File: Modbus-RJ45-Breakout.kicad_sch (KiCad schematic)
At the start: 99 parts, among them J1 RJ45_Weidmueller_2562920000, J2 RJ45_Weidmueller_2562920000, J3 Conn_01x04, J4 Conn_01x04, J5 USB_B_Mini, U2 WE-TVS-82400102, U3 MAX485E, U4 ADM2687E, U7 MAX485E, U8 ADM2687E

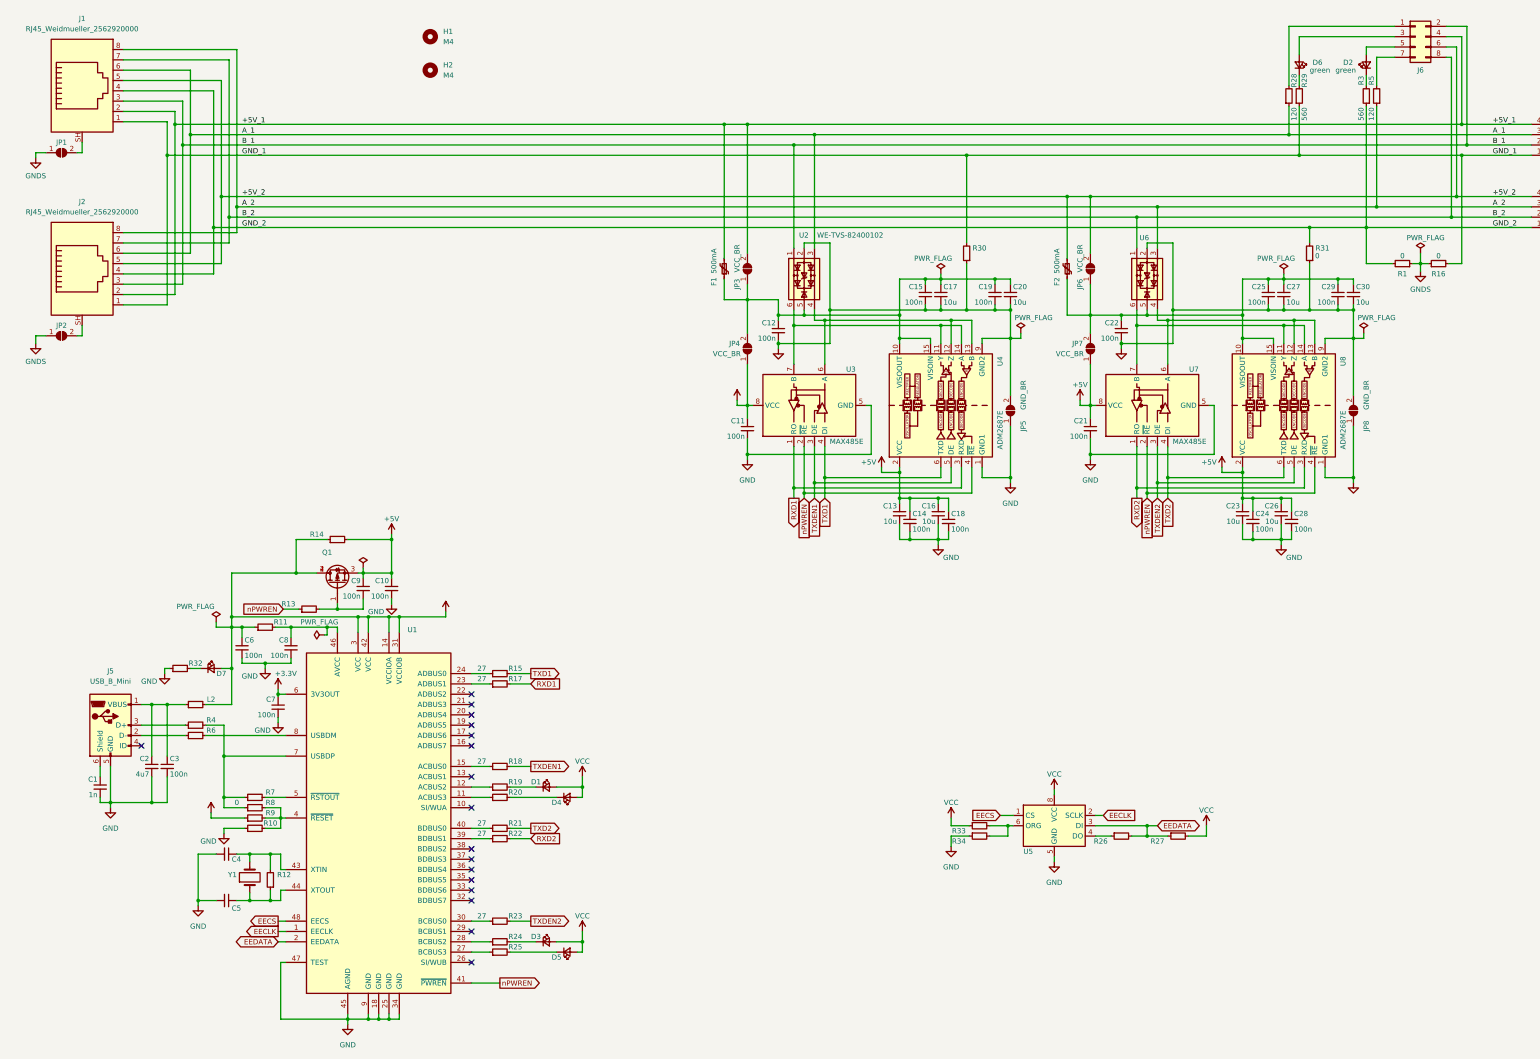
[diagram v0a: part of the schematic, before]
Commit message: Partly improved and re-routed
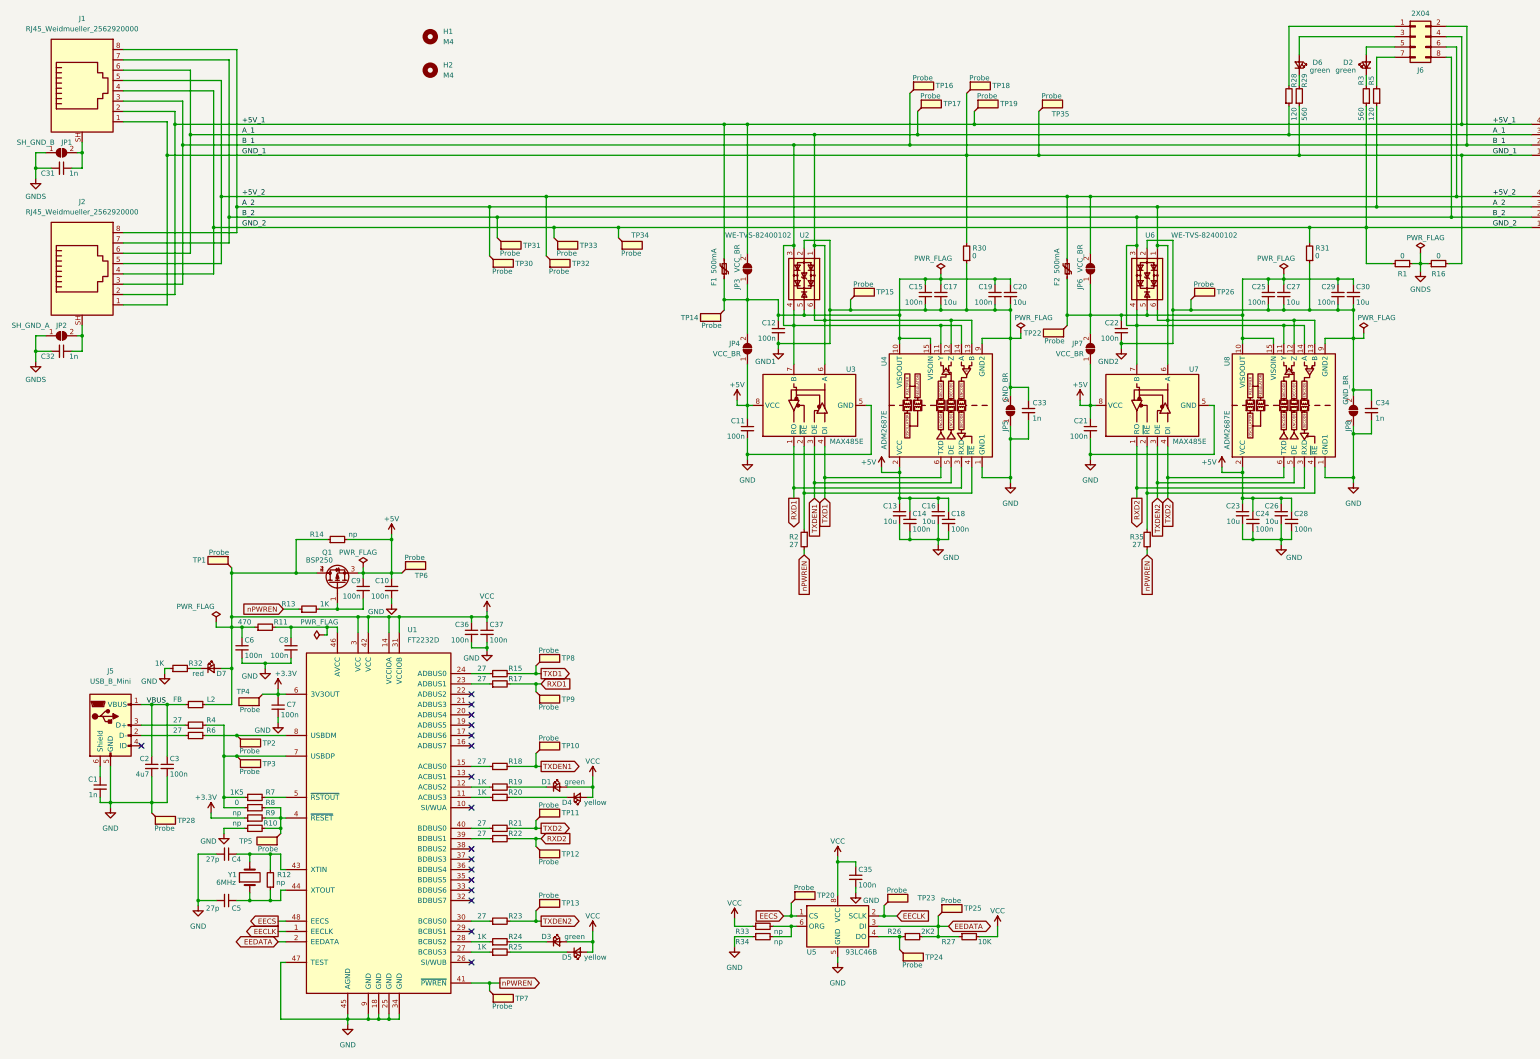
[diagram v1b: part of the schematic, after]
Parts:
- added C31, C32, C33, C34: 1n, Capacitor_SMD:C_1206_3216Metric_Pad1.33x1.80mm_HandSolder, symbol Device:C_Small
- added C35, C36, C37: 100n, Capacitor_SMD:C_0603_1608Metric_Pad1.08x0.95mm_HandSolder, symbol Device:C_Small
- added R2, R35: 27, Resistor_SMD:R_0603_1608Metric_Pad0.98x0.95mm_HandSolder, symbol Device:R_Small
- added TP1, TP28, TP34, TP35, TP6: Probe, TestPoint:TestPoint_THTPad_2.0x2.0mm_Drill1.0mm, symbol Connector:TestPoint_Flag
- added TP10, TP11, TP12, TP13, TP14, TP15, TP16, TP17, TP18, TP19, TP2, TP20, TP22, TP23, TP24, TP25, TP26, TP3, TP30, TP31, TP32, TP33, TP4, TP5, TP7, TP8, TP9: Probe, TestPoint:TestPoint_Pad_D1.5mm, symbol Connector:TestPoint_Flag
- C4, C5: value (none) -> 27p; footprint (none) -> Capacitor_SMD:C_0603_1608Metric_Pad1.08x0.95mm_HandSolder
- D1, D3: value (none) -> green; footprint (none) -> LED_SMD:LED_0603_1608Metric_Pad1.05x0.95mm_HandSolder
- D4, D5: value (none) -> yellow; footprint (none) -> LED_SMD:LED_0603_1608Metric_Pad1.05x0.95mm_HandSolder
- D7: value (none) -> red; footprint (none) -> LED_SMD:LED_0603_1608Metric_Pad1.05x0.95mm_HandSolder
- J3, J4: footprint Connector_Wago:Wago_734-164_1x04_P3.50mm_Horizontal -> the78mole:Wago_734-164_1x04_P3.50mm_Horizontal
- J5: footprint Connector_USB:USB_Mini-B_Wuerth_65100516121_Horizontal -> the78mole:USB_Mini-B_Wuerth_65100516121_Horizontal
- J6: value (none) -> 2X04; footprint (none) -> Connector_PinHeader_2.54mm:PinHeader_2x04_P2.54mm_Vertical_SMD
- JP1: value (none) -> SH_GND_B; footprint (none) -> Jumper:SolderJumper-2_P1.3mm_Open_TrianglePad1.0x1.5mm
- JP2: value (none) -> SH_GND_A; footprint (none) -> Jumper:SolderJumper-2_P1.3mm_Open_TrianglePad1.0x1.5mm
- L2: value (none) -> FB; footprint (none) -> Resistor_SMD:R_0603_1608Metric_Pad0.98x0.95mm_HandSolder
- Q1: value (none) -> BSP250; footprint (none) -> Package_TO_SOT_SMD:SOT-223
- R10, R12, R14, R33, R34, R9: value (none) -> np; footprint (none) -> Resistor_SMD:R_0603_1608Metric_Pad0.98x0.95mm_HandSolder
- R11: value (none) -> 470; footprint (none) -> Resistor_SMD:R_0603_1608Metric_Pad0.98x0.95mm_HandSolder
- R13, R19, R20, R24, R25, R32: value (none) -> 1K; footprint (none) -> Resistor_SMD:R_0603_1608Metric_Pad0.98x0.95mm_HandSolder
- R26: value (none) -> 2K2; footprint (none) -> Resistor_SMD:R_0603_1608Metric_Pad0.98x0.95mm_HandSolder
- R27: value (none) -> 10K; footprint (none) -> Resistor_SMD:R_0603_1608Metric_Pad0.98x0.95mm_HandSolder
- R30: value (none) -> 0; footprint (none) -> Resistor_SMD:R_0603_1608Metric_Pad0.98x0.95mm_HandSolder
- R4, R6: value (none) -> 27; footprint (none) -> Resistor_SMD:R_0603_1608Metric_Pad0.98x0.95mm_HandSolder
- R7: value (none) -> 1K5; footprint (none) -> Resistor_SMD:R_0603_1608Metric_Pad0.98x0.95mm_HandSolder
- U1: value (none) -> FT2232D; footprint (none) -> Package_QFP:LQFP-48_7x7mm_P0.5mm
- U5: value (none) -> 93LC46B; footprint (none) -> Package_SO:SOIC-8_3.9x4.9mm_P1.27mm
- U6: value (none) -> WE-TVS-82400102; footprint (none) -> Package_TO_SOT_SMD:SOT-23-6
- Y1: value (none) -> 6MHz; footprint (none) -> Crystal:Crystal_SMD_HC49-SD_HandSoldering
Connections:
- net +3V3: now also TP4.1
- net +5V: now also TP6.1
- net +5V_1: now also TP19.1
- net +5V_2: now also TP32.1
- net A_1: now also U2.1, U2.6, U3.6 (A), U4.12 (Z), U4.13 (B), TP17.1; no longer U2.3
- net A_2: now also U6.1, U6.6, U7.6 (A), U8.12 (Z), U8.13 (B), TP30.1; no longer U6.3
- net B_1: now also U2.3, U2.4, U3.7 (B), U4.11 (Y), U4.14 (A), TP16.1; no longer U2.1
- net B_2: now also U6.3, U6.4, U7.7 (B), U8.11 (Y), U8.14 (A), TP31.1; no longer U6.1
- net EECLK: now also TP23.1
- net EECS: now also TP20.1
- net EEDATA: now also TP25.1
- net GND: now also C33.2, C34.2, C35.2, C36.2, C37.2, TP28.1
- net GND1: now also C33.1, TP15.1
- net GND2: now also C34.1, TP26.1
- net GNDS: now also C31.2, C32.2
- net GND_1: now also TP18.1, TP35.1
- net GND_2: now also TP33.1, TP34.1
- net RXD1: now also TP9.1
- net RXD2: now also TP12.1
- net TXD1: now also TP8.1
- net TXD2: now also TP11.1
- net TXDEN1: now also TP10.1
- net TXDEN2: now also TP13.1
- net VCC: now also C35.1, C36.1, C37.1, TP1.1
- net nPWREN: now also R2.2, R35.2, TP7.1; no longer U3.2 (~{RE}), U4.4 (~{RE}), U7.2 (~{RE}), U8.4 (~{RE})
- net at C12.1, C15.1, C17.1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: now also TP14.1
- net at C22.1, C25.1, C27.1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: now also TP22.1
- net at R4.2, R7.1, R8.1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: now also TP3.1
- net at R10.2, R8.2, R9.2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: now also TP5.1
- net at J1.SH, JP1.2 (B): now also C31.1
- net at R26.1, U5.4 (DO): now also TP24.1
- net VBUS: now reaches C2.1, C3.1, J5.1 (VBUS), L2.1
- net at J2.SH, JP2.2 (B): now also C32.1
- net at R6.2, U1.8 (USBDM): now also TP2.1
- new net: R35.1, U7.2 (~{RE}), U8.4 (~{RE})
- new net: R2.1, U3.2 (~{RE}), U4.4 (~{RE})
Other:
- moved on the sheet: D1, D3, D4, D5, R26, R27, R33, R34, U2, U5, U6

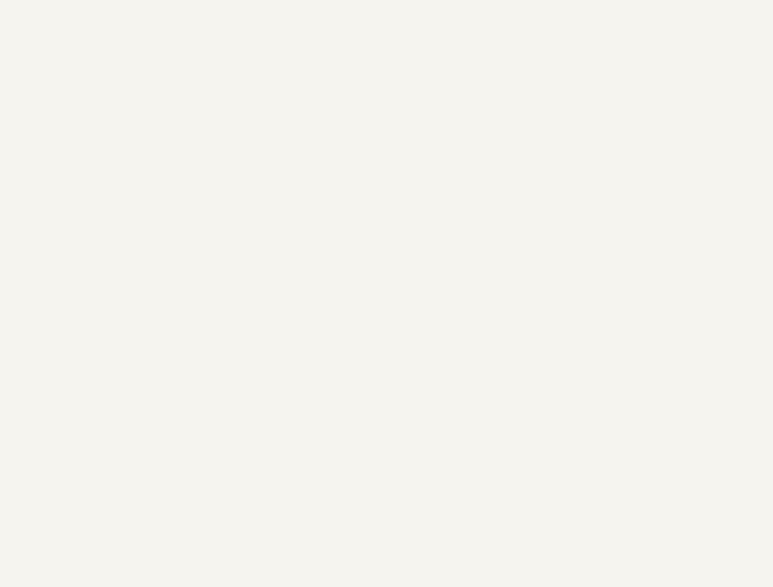
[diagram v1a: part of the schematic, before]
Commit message: As ordered, added info on enclosures
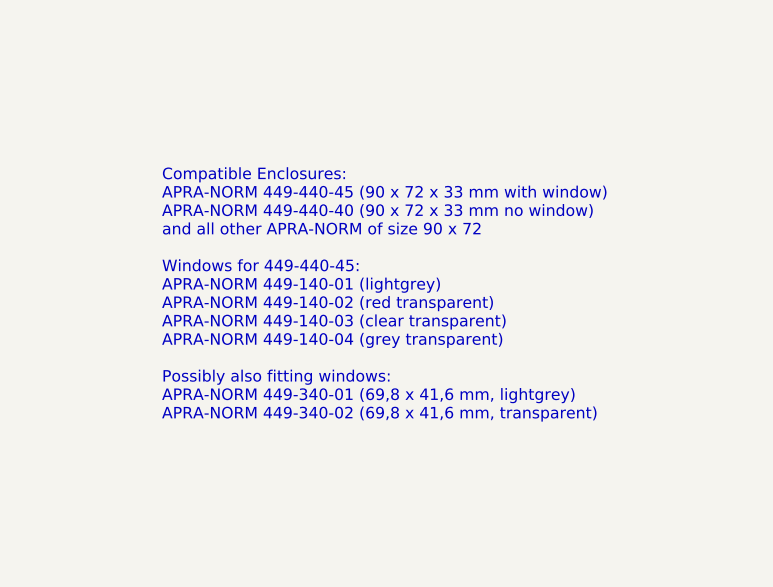
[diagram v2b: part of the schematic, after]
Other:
- note added: "Compatible Enclosures: APRA-NORM 449-440-45 (90 x 72 x 33 mm with window) APRA-NORM 449-440-40 (90 x 72 x 33 mm no window) and all other APRA-NORM of size 90 x 72 Windows for 449-440-45: APRA-NORM 449-140-01 (lightgrey) APRA-NORM 449-140-02 (red transparent) APRA-NORM 449-140-03 (clear transparent) APRA-NORM 449-140-04 (grey transparent) Possibly also fitting windows: APRA-NORM 449-340-01 (69,8 x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"
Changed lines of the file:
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@@
     (stroke (width 0) (type default) (color 0 0 0 0))
+  )
+  (text "Compatible Enclosures:\nAPRA-NORM 449-440-45 (90 x 72 x 33 mm with window)\nAPRA-NORM 449-440-40 (90 x 72 x 33 mm no window)\nand all other APRA-NORM of size 90 x 72\n\nWindows for 449-440-45:\nAPRA-NORM 449-140-01 (lightgrey)\nAPRA-NORM 449-140-02 (red transparent)\nAPRA-NORM 449-140-03 (clear transparent)\nAPRA-NORM 449-140-04 (grey transparent)\n\nPossibly also fitting windows:\nAPRA-NORM 449-340-01 (69,8 x 41,6 mm, lightgrey)\nAPRA-NORM 449-340-02 (69,8 x 41,6 mm, transparent)\n\n\n"
+    (at 343.535 250.825 0)
+    (effects (font (size 1.27 1.27)) (justify left bottom))
   )
   (label "VBUS" (at 45.72 185.42 0)

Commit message: Fixed TP docs on PCB and added ibom
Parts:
- Y1: Reichelt (none) -> IQD LFXTAL016788
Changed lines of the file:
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@@
+      (effects (font (size 1.27 1.27)) hide)
+    )
+    (property "Reichelt" "IQD LFXTAL016788" (id 7) (at 71.12 227.965 90)
       (effects (font (size 1.27 1.27)) hide)
     )

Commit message: Adjustments during prototype build
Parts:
- R29, R3: value 560 -> (none); footprint Resistor_SMD:R_0603_1608Metric_Pad0.98x0.95mm_HandSolder -> (none)
- R8: value 0 -> (none); footprint Resistor_SMD:R_0603_1608Metric_Pad0.98x0.95mm_HandSolder -> (none)
- R9: value np -> (none); footprint Resistor_SMD:R_0603_1608Metric_Pad0.98x0.95mm_HandSolder -> (none)
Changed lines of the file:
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@@
     (in_bom yes) (on_board yes)
     (property "Reference" "R8" (id 0) (at 76.2 209.55 90))
-    (property "Value" "0" (id 1) (at 67.945 209.55 90))
-    (property "Footprint" "Resistor_SMD:R_0603_1608Metric_Pad0.98x0.95mm_HandSolder" (id 2) (at 72.39 210.82 0)
+    (property "Value" "" (id 1) (at 67.945 209.55 90))
+    (property "Footprint" "" (id 2) (at 72.39 210.82 0)
       (effects (font (size 1.27 1.27)) hide)
     )
@@
     (in_bom yes) (on_board yes)
     (property "Reference" "R3" (id 0) (at 344.805 31.75 90))
-    (property "Value" "560" (id 1) (at 344.805 40.005 90))
-    (property "Footprint" "Resistor_SMD:R_0603_1608Metric_Pad0.98x0.95mm_HandSolder" (id 2) (at 346.075 35.56 0)
+    (property "Value" "" (id 1) (at 344.805 40.005 90))
+    (property "Footprint" "" (id 2) (at 346.075 35.56 0)
       (effects (font (size 1.27 1.27)) hide)
     )
@@
     (in_bom yes) (on_board yes)
     (property "Reference" "R29" (id 0) (at 330.835 31.75 90))
-    (property "Value" "560" (id 1) (at 330.835 40.005 90))
-    (property "Footprint" "Resistor_SMD:R_0603_1608Metric_Pad0.98x0.95mm_HandSolder" (id 2) (at 329.565 35.56 0)
+    (property "Value" "" (id 1) (at 330.835 40.005 90))
+    (property "Footprint" "" (id 2) (at 329.565 35.56 0)
       (effects (font (size 1.27 1.27)) hide)
     )
@@
     (in_bom yes) (on_board yes)
     (property "Reference" "R9" (id 0) (at 76.2 212.09 90))
-    (property "Value" "np" (id 1) (at 67.945 212.09 90))
-    (property "Footprint" "Resistor_SMD:R_0603_1608Metric_Pad0.98x0.95mm_HandSolder" (id 2) (at 72.39 213.36 0)
+    (property "Value" "" (id 1) (at 67.945 212.09 90))
+    (property "Footprint" "" (id 2) (at 72.39 213.36 0)
       (effects (font (size 1.27 1.27)) hide)
     )
@@
     )
     (path "/14c667e2-48bf-486f-835f-2bfc8b1b68a9"
-      (reference "R3") (unit 1) (value "560") (footprint "Resistor_SMD:R_0603_1608Metric_Pad0.98x0.95mm_HandSolder")
+      (reference "R3") (unit 1) (value "1K") (footprint "Resistor_SMD:R_0603_1608Metric_Pad0.98x0.95mm_HandSolder")
     )
     (path "/ffba077d-789a-43fd-9690-fea8d1c6c6e3"
@@
     )
     (path "/0ce16148-6e5c-406f-b93f-5f9bdea40745"
-      (reference "R8") (unit 1) (value "0") (footprint "Resistor_SMD:R_0603_1608Metric_Pad0.98x0.95mm_HandSolder")
+      (reference "R8") (unit 1) (value "np") (footprint "Resistor_SMD:R_0603_1608Metric_Pad0.98x0.95mm_HandSolder")
     )
     (path "/e9bfecd0-abec-4635-bba6-51fe95cde897"
-      (reference "R9") (unit 1) (value "np") (footprint "Resistor_SMD:R_0603_1608Metric_Pad0.98x0.95mm_HandSolder")
+      (reference "R9") (unit 1) (value "1K5") (footprint "Resistor_SMD:R_0603_1608Metric_Pad0.98x0.95mm_HandSolder")
     )
     (path "/b78bd01a-2206-46d8-905f-796ed73c744b"
@@
     )
     (path "/88437f4a-27c1-4b04-98c4-1a971c51d440"
-      (reference "R29") (unit 1) (value "560") (footprint "Resistor_SMD:R_0603_1608Metric_Pad0.98x0.95mm_HandSolder")
+      (reference "R29") (unit 1) (value "1K") (footprint "Resistor_SMD:R_0603_1608Metric_Pad0.98x0.95mm_HandSolder")
     )
     (path "/ec52c643-6bf7-4767-a00c-6c226ebdebc9"

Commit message: RS485 bus echo solved and A<->B swap with ISO Transceivers (schematic only)
This can be solved also with the current PCB by swapping the A and B externally
and not mixing ISO and non-ISO bus transceivers. The RX-Enable problem can be solved
by a desoldering R2 and R35 and bridging the pads to R18 and R23 resp. close to the transceiver.
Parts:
- added R? (x2): 27, Resistor_SMD:R_0603_1608Metric_Pad0.98x0.95mm_HandSolder, symbol Device:R_Small
- R2: value 27 -> (none); footprint Resistor_SMD:R_0603_1608Metric_Pad0.98x0.95mm_HandSolder -> (none)
- R29, R3: value (none) -> 1K; footprint (none) -> Resistor_SMD:R_0603_1608Metric_Pad0.98x0.95mm_HandSolder
- R35: value 27 -> (none); footprint Resistor_SMD:R_0603_1608Metric_Pad0.98x0.95mm_HandSolder -> (none); NP (none) -> np
- R8: value (none) -> np; footprint (none) -> Resistor_SMD:R_0603_1608Metric_Pad0.98x0.95mm_HandSolder
- R9: value (none) -> 1K5; footprint (none) -> Resistor_SMD:R_0603_1608Metric_Pad0.98x0.95mm_HandSolder
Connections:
- net A_1: now also U4.11 (Y), U4.14 (A); no longer U4.12 (Z), U4.13 (B)
- net A_2: now also U8.11 (Y), U8.14 (A); no longer U8.12 (Z), U8.13 (B)
- net B_1: now also U4.12 (Z), U4.13 (B); no longer U4.11 (Y), U4.14 (A)
- net B_2: now also U8.12 (Z), U8.13 (B); no longer U8.11 (Y), U8.14 (A)
- net TXDEN1: now also R?.2
- net TXDEN2: now also R?.2
- net at R35.1, U7.2 (~{RE}), U8.4 (~{RE}): now also R?.1
- net at R2.1, U3.2 (~{RE}), U4.4 (~{RE}): now also R?.1
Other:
- note added: "TODO: Update PCB"
- note added: "This is just optional, if you want to provide a different manufacturer or device identifier or want to change the maximum current drawn from USB bus. To program it, you can get the FT_PROG - EEPROM Programming Utility from FTDI (current version: 3.12.31.639). https://ftdichip.com/utilities/"
- note added: "This is the suggested solution from FT2232D datasheet to get RS485 interfaces. But it does not work well with wide spread ModBus libraries, which can not filter the echo from the bus. Therefore, the RX-enable (nRE) must be connected with TX-enable (DI/DE) to mask the transmit data from RX."
- moved on the sheet: R2, R35

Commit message: Fixed all issues and added Gerber exports
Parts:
- added DRA1: APRA 449-440-45, symbol Mechanical:DIN_Rail_Adapter
- added J7: WAGO 2734-104, symbol Connector:Conn_01x04_Female
- added J8: (no value), symbol Connector:Conn_01x04_Female
- J3: value Conn_01x04 -> Bus_2
- J4: value Conn_01x04 -> BUS_1
- R2, R35: value (none) -> np; footprint (none) -> Resistor_SMD:R_0603_1608Metric_Pad0.98x0.95mm_HandSolder
- gave numbers to parts that had none: 2
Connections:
- net A_2: now also U6.3, U6.4; no longer U6.1, U6.6
- net B_2: now also U6.1, U6.6; no longer U6.3, U6.4
- no-connect marks 17 -> 25
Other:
- note added: "Mating connectors: 2 x WAGO 2734-104"
- note added: "R2 and R35 have been the suggested solution from FT2232D datasheet to realize RS485 interfaces. But it does not work well with wide spread ModBus SW libraries, which can not filter the echo from the bus. Therefore, the RX-enable (nRE) must be connected with TX-enable (DI/DE) by R36 and R37 to mask the transmit data from RX."
- note added: "When using the isolated RS485 Transceiver (ADM2687E) it is not recommended to bridge the power to the bus. This has two reasons: 1. The power capability of the ISO power is 55 mA while the requirement of the isolated side can reach up to 55 mA on worst operating conditions (highest data rate (16 MBps), highest operating temperature and lowest termination: 54 Ohms total = 2 x 120 Ohms + loads 2. T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"
- note removed: "TODO: Update PCB"
- note removed: "This is the suggested solution from FT2232D datasheet to get RS485 interfaces. But it does not work well with wide spread ModBus libraries, which can not filter the echo from the bus. Therefore, the RX-enable (nRE) must be connected with TX-enable (DI/DE) to mask the transmit data from RX."
- moved on the sheet: R2, R36, U6
